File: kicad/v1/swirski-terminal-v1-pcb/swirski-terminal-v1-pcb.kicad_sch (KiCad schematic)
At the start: 15 parts, among them U1 Coin_Vibration_Motor, U1 Seeed_Lipo_Rider_Plus, U2 MAX17048

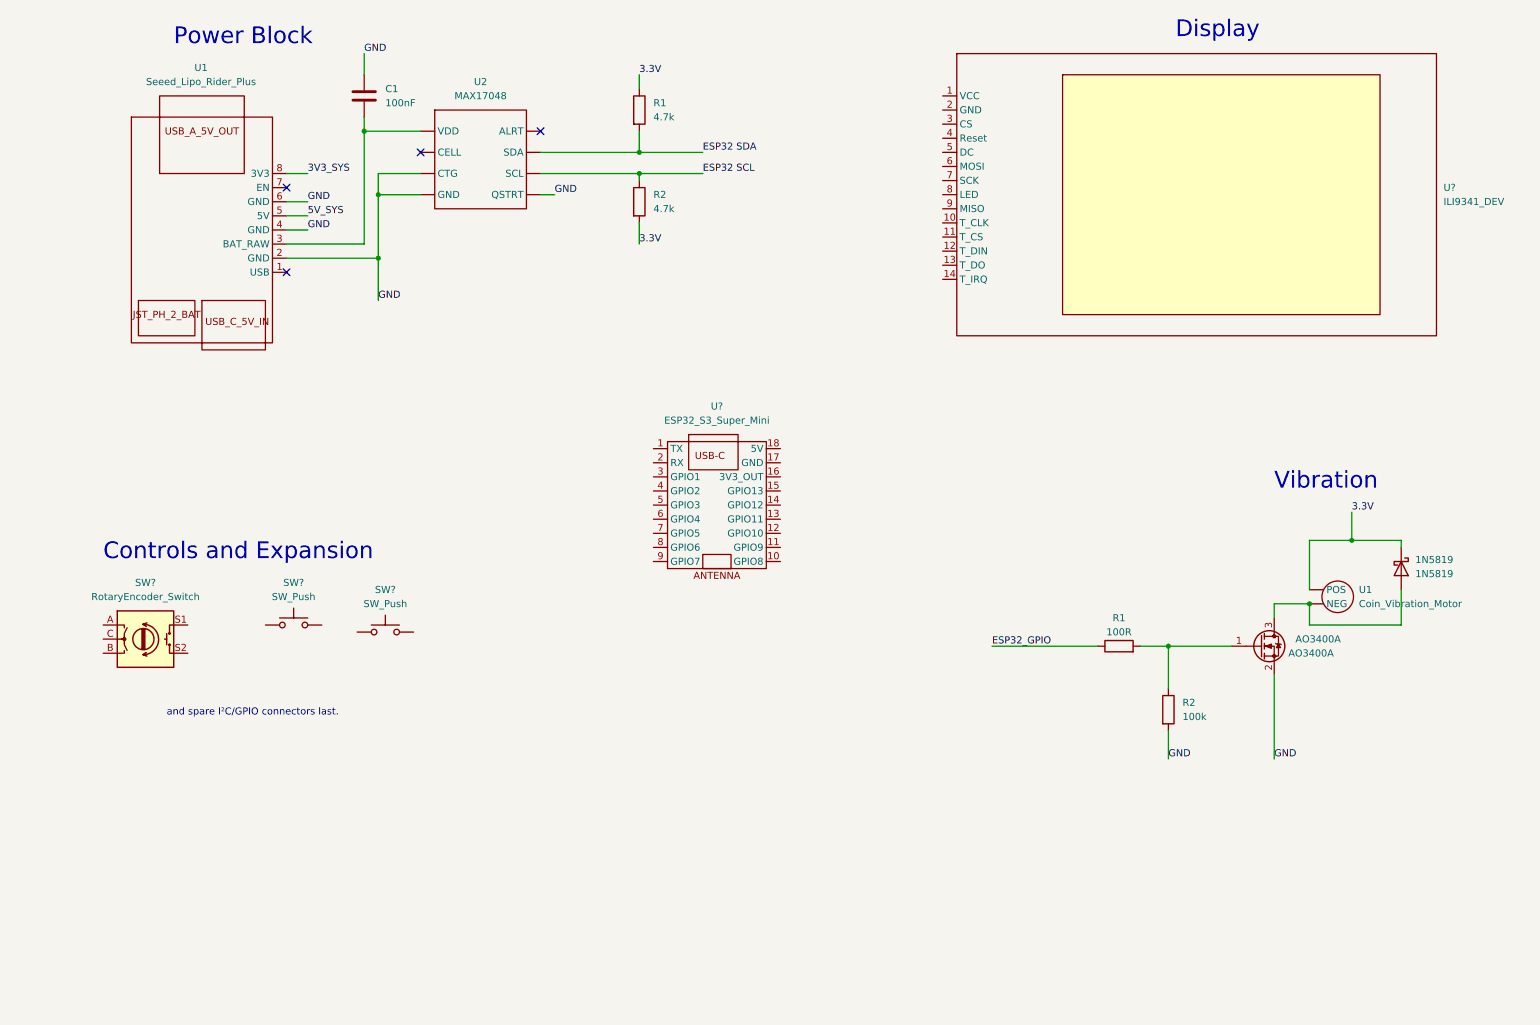
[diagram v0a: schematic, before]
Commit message: updated swirski terminal schematic!
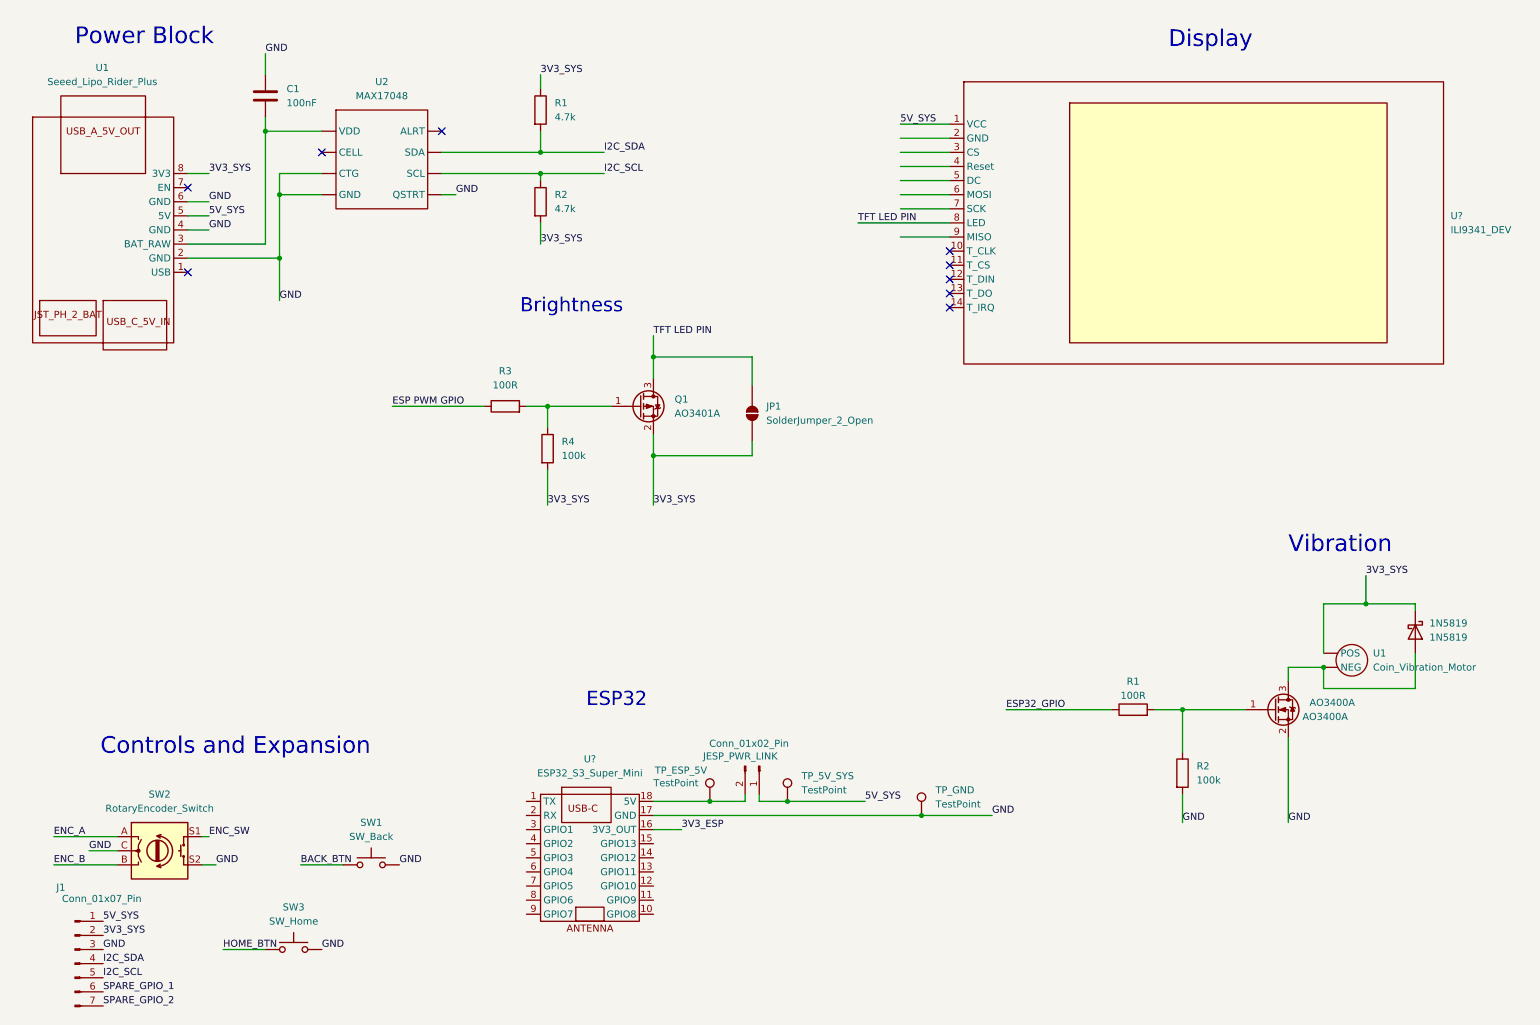
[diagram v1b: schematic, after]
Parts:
- added J1: Conn_01x07_Pin, symbol Connector:Conn_01x07_Pin
- added JESP_PWR_LINK: Conn_01x02_Pin, symbol Connector:Conn_01x02_Pin
- added JP1: SolderJumper_2_Open, symbol Jumper:SolderJumper_2_Open
- added Q1: AO3401A, Package_TO_SOT_SMD:SOT-23, symbol Transistor_FET:AO3401A
- added R3: 100R, symbol Device:R
- added R4: 100k, symbol Device:R
- added TP_5V_SYS, TP_ESP_5V, TP_GND: TestPoint, symbol Connector:TestPoint
- SW1: renamed from SW?; value SW_Push -> SW_Back
- SW3: renamed from SW?; value SW_Push -> SW_Home
- gave numbers to parts that had none: 1
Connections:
- net 3.3V is gone; now on net 3V3_SYS: 1N5819.1 (K), R1.1, R2.2, U1. (NEG)
- net ESP32 SDA is gone; now on net I2C_SDA: R1.2, U2. (QSTRT)
- net 3V3_SYS: now also J1.2 (Pin_2), JP1.1 (A), Q1.2 (S), R4.2
- net 5V_SYS: now also U?.1 (VCC), J1.1 (Pin_1), JESP_PWR_LINK.1 (Pin_1), TP_5V_SYS.1
- net GND: now also SW1.2, SW2.C, SW2.S2, SW3.2, U?.17 (GND), J1.3 (Pin_3), TP_GND.1
- net ENC_A: now reaches SW2.A
- net ENC_B: now reaches SW2.B
- net ENC_SW: now reaches SW2.S1
- net HOME_BTN: now reaches SW3.1
- net 3V3_ESP: now reaches U?.16 (3V3_OUT)
- net at U?.18 (5V): now also JESP_PWR_LINK.2 (Pin_2), TP_ESP_5V.1
- net TFT LED PIN: now reaches U?.8 (LED)
- net TFT LED PIN: now also JP1.2 (B), Q1.3 (D)
- net I2C_SDA: now reaches U2. (QSTRT)
- net I2C_SDA: now also J1.4 (Pin_4)
- net BACK_BTN: now reaches SW1.1
- net ESP32 SCL  renamed I2C_SCL
- net I2C_SCL: now also J1.5 (Pin_5)
- new net: Q1.1 (G), R3.2, R4.1
- new net ESP PWM GPIO: R3.1
- new net SPARE_GPIO_1: J1.6 (Pin_6)
- new net SPARE_GPIO_2: J1.7 (Pin_7)
- no-connect marks 4 -> 9
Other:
- note added: "Brightness"
- note added: "ESP32"
- note removed: "and spare I²C/GPIO connectors last."
- moved on the sheet: 1N5819, AO3400A, C1, R1, R2, SW1, SW2, SW3, U1, U2, U?

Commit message: PCB Updates
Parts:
- added C2, C4, C6, C8: 100nF, symbol Device:C
- added C3, C5, C7: 10µF, symbol Device:C
- added R5: 10k, symbol pspice:R
- added TP_3V3_ESP, TP_3V3_SYS, TP_BAT_RAW: TestPoint, symbol Connector:TestPoint
- added U3: MCP23008-xSO, Package_SO:SOIC-18W_7.5x11.6mm_P1.27mm, symbol Interface_Expansion:MCP23008-xSO
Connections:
- net ESP PWM GPIO is gone; now on net TFT_BL_PWM: R3.1
- net ESP32_GPIO is gone; now on net VIB_EN: R1.1
- net SPARE_GPIO_1 is gone; now on net ESP_SPARE_A: J1.6 (Pin_6)
- net 3V3_ESP: now also J1.2 (Pin_2), R1.1, R2.2, C2.1, R5.1, TP_3V3_ESP.1, U3.18 (VDD)
- net 3V3_SYS: now also C5.1, C6.1, C7.1, C8.1, TP_3V3_SYS.1; no longer J1.2 (Pin_2), R1.1, R2.2
- net 5V_SYS: now also C3.2, C4.2
- net BACK_BTN: now also U3.11 (GP1)
- net ENC_A: now also U?.13 (GPIO11)
- net ENC_B: now also U?.12 (GPIO10)
- net ENC_SW: now also U3.10 (GP0)
- net GND: now also U?.2 (GND), C2.2, C3.1, C4.1, C5.2, C6.2, C7.2, C8.2, U3.3 (A2), U3.4 (A1), U3.5 (A0), U3.9 (VSS)
- net HOME_BTN: now also U3.12 (GP2)
- net I2C_SCL: now also U?.3 (GPIO1), U3.1 (SCL)
- net I2C_SDA: now also U?.4 (GPIO2), U3.2 (SDA)
- net LCD_PIN_RST: now reaches U?.10 (GPIO8)
- net LCD_PIN_RST: now also U?.4 (Reset)
- net ESP_SPARE_A: now reaches U?.11 (GPIO9)
- net TFT_BL_PWM: now reaches U?.14 (GPIO12)
- net VIB_EN: now reaches U?.15 (GPIO13)
- net LCD_PIN_DC: now reaches U?.6 (GPIO4)
- net LCD_PIN_DC: now also U?.5 (DC)
- net LCD_PIN_CS: now reaches U?.7 (GPIO5)
- net LCD_PIN_CS: now also U?.3 (CS)
- net LCD_PIN_MOSI: now reaches U?.8 (GPIO6)
- net LCD_PIN_MOSI: now also U?.6 (MOSI)
- net LCD_PIN_SCLK: now reaches U?.9 (GPIO7)
- net LCD_PIN_SCLK: now also U?.7 (SCK)
- net at C1.2, U1.3 (BAT_RAW), U2. (QSTRT): now also TP_BAT_RAW.1
- net SPARE_GPIO_2 renamed EXTRA_GPIO_1
- net EXTRA_GPIO_1: now also U3.13 (GP3)
- new net: R5.2, U3.6 (~{RESET})
- new net EXTRA_GPIO_2: U3.14 (GP4)
- new net EXTRA_GPIO_3: U3.15 (GP5)
- new net EXTRA_GPIO_4: U3.16 (GP6)
- new net EXTRA_OUTPUT: U3.17 (GP7)
- no-connect marks 9 -> 14
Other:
- note added: "GPIO EXPANSION INTERNAL"
- moved on the sheet: JP1, Q1, R1, R2, R3, R4, TP_GND

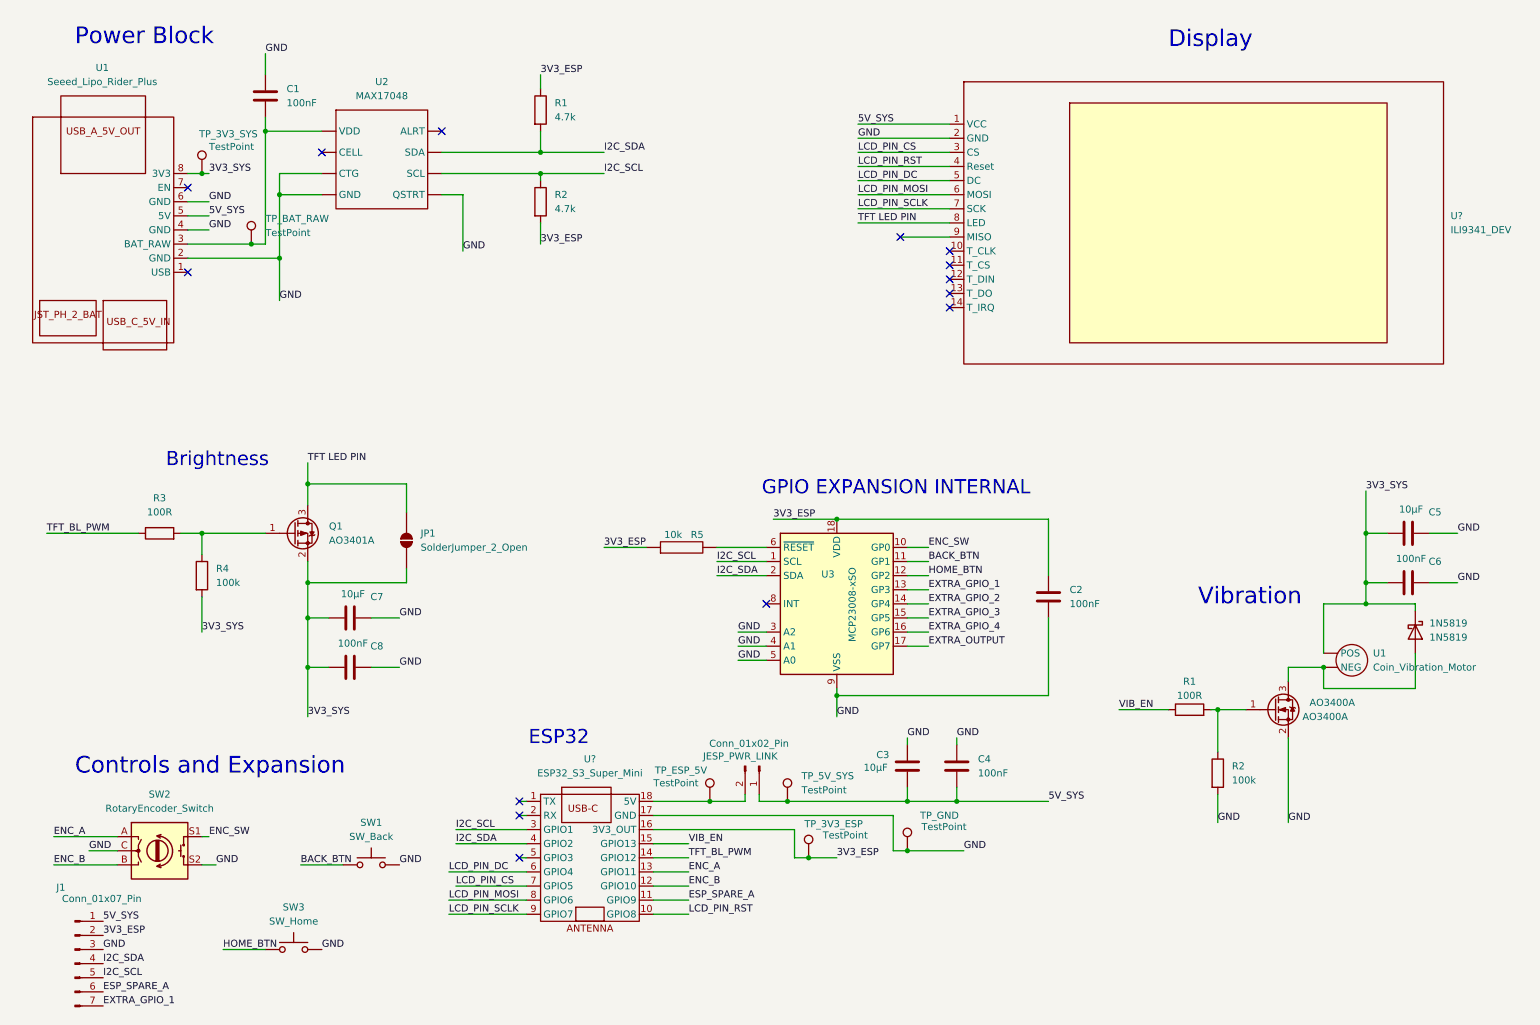
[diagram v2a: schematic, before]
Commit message: More Kicad updates - playing around with the schematic and replacing SMD components that were being used on the PCB
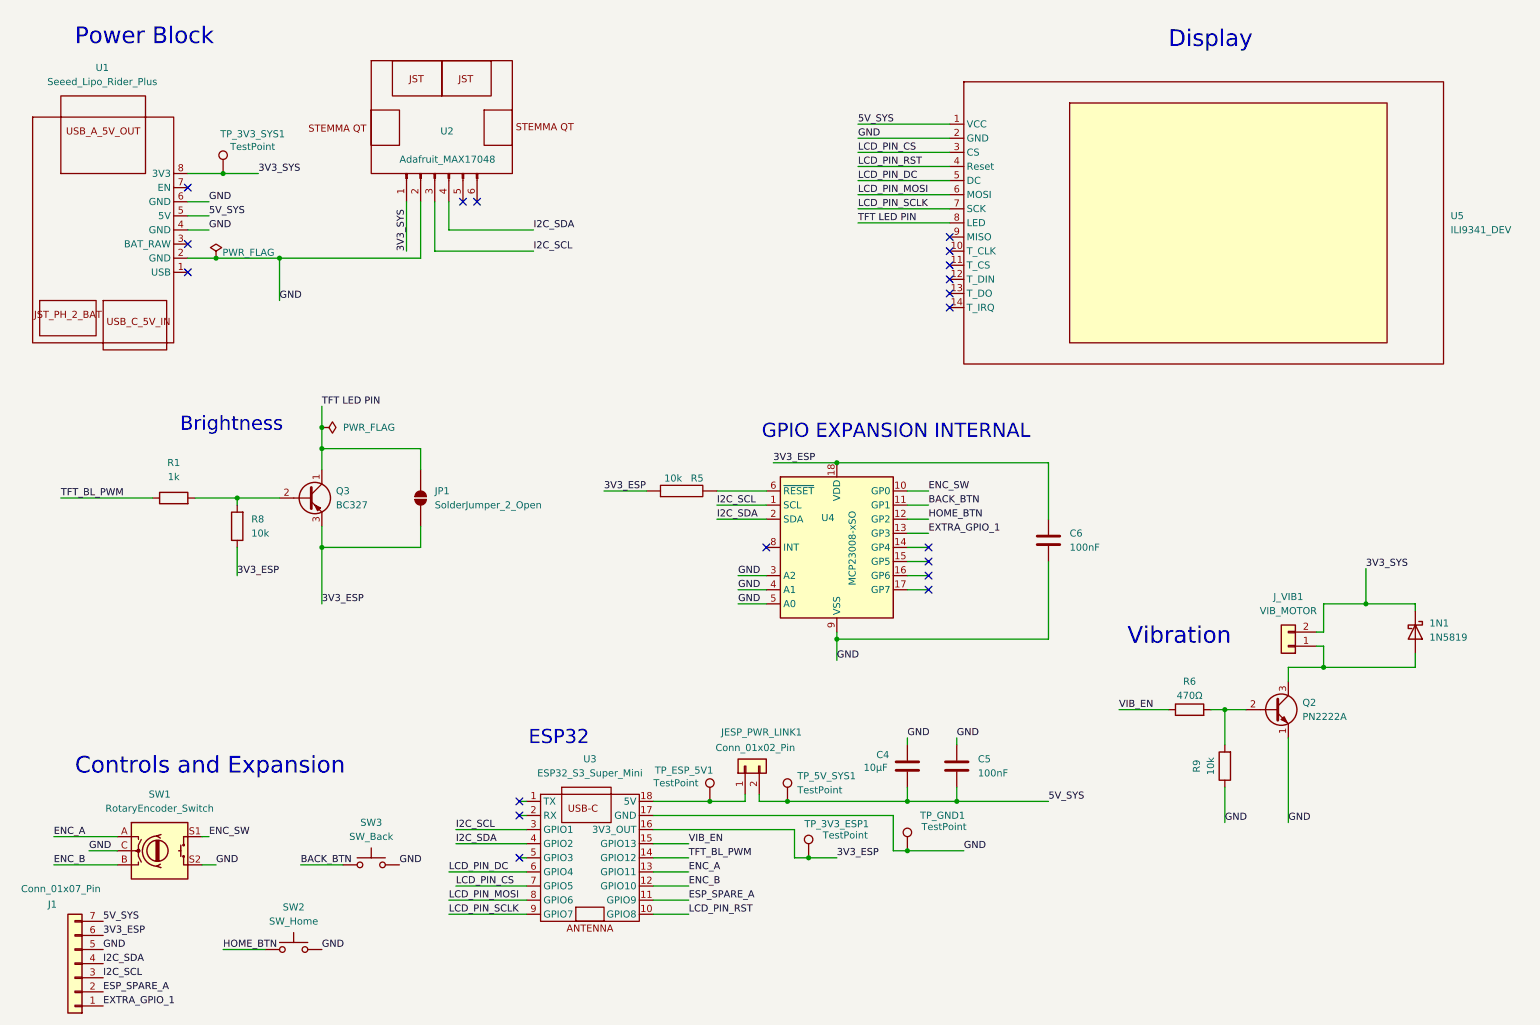
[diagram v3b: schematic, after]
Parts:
- removed AO3400A: AO3400A, Package_TO_SOT_SMD:SOT-23, symbol Transistor_FET:AO3400A
- removed C1, C6, C8: 100nF, symbol Device:C
- removed C5, C7: 10µF, symbol Device:C
- removed Q1: AO3401A, Package_TO_SOT_SMD:SOT-23, symbol Transistor_FET:AO3401A
- removed R1, R2: 4.7k, symbol Device:R
- removed R2, R4: 100k, symbol Device:R
- removed TP_BAT_RAW: TestPoint, symbol Connector:TestPoint
- removed U1: Coin_Vibration_Motor, symbol Swirski_Terminal:Coin_Vibration_Motor
- removed U2: MAX17048, symbol Swirski_Terminal:MAX17048
- added J_VIB1: VIB_MOTOR, Connector_PinHeader_2.54mm:PinHeader_1x02_P2.54mm_Vertical, symbol Connector_Generic:Conn_01x02
- added Q2: PN2222A, Package_TO_SOT_THT:TO-92_Inline, symbol Transistor_BJT:PN2222A
- added Q3: BC327, Package_TO_SOT_THT:TO-92_Inline, symbol Transistor_BJT:BC327
- added R8, R9: 10k, Resistor_THT:R_Axial_DIN0207_L6.3mm_D2.5mm_P10.16mm_Horizontal, symbol Device:R
- added U2: Adafruit_MAX17048, Swirski_Terminal:Adafruit_MAX17048_Breakout, symbol Swirski_Terminal:Adafruit_MAX17048
- C4: renamed from C3; footprint (none) -> Capacitor_THT:CP_Radial_D5.0mm_P2.00mm
- C5: renamed from C4; footprint (none) -> Capacitor_THT:C_Disc_D5.0mm_W2.5mm_P5.00mm
- C6: renamed from C2; footprint (none) -> Capacitor_THT:C_Disc_D5.0mm_W2.5mm_P5.00mm
- J1: footprint (none) -> Connector_PinHeader_2.54mm:PinHeader_1x07_P2.54mm_Vertical; symbol Connector:Conn_01x07_Pin -> Connector_Generic:Conn_01x07
- JESP_PWR_LINK1: renamed from JESP_PWR_LINK; footprint (none) -> Connector_PinHeader_2.54mm:PinHeader_1x02_P2.54mm_Vertical; symbol Connector:Conn_01x02_Pin -> Connector_Generic:Conn_01x02
- JP1: footprint (none) -> Connector_PinHeader_2.54mm:PinHeader_1x02_P2.54mm_Vertical
- R1: renamed from R3; value 100R -> 1k; footprint (none) -> Resistor_THT:R_Axial_DIN0207_L6.3mm_D2.5mm_P10.16mm_Horizontal
- R5: footprint (none) -> Resistor_THT:R_Axial_DIN0207_L6.3mm_D2.5mm_P10.16mm_Horizontal
- R6: renamed from R1; value 100R -> 470Ω; footprint (none) -> Resistor_THT:R_Axial_DIN0207_L6.3mm_D2.5mm_P10.16mm_Horizontal
- SW1: renamed from SW2; footprint (none) -> Rotary_Encoder:RotaryEncoder_Alps_EC11E-Switch_Vertical_H20mm
- SW2: renamed from SW3; footprint (none) -> Button_Switch_THT:SW_PUSH_6mm
- SW3: renamed from SW1; footprint (none) -> Button_Switch_THT:SW_PUSH_6mm
- TP_3V3_ESP1: renamed from TP_3V3_ESP; footprint (none) -> TestPoint:TestPoint_Loop_D2.50mm_Drill1.0mm
- TP_3V3_SYS1: renamed from TP_3V3_SYS; footprint (none) -> TestPoint:TestPoint_Loop_D2.50mm_Drill1.0mm
- TP_5V_SYS1: renamed from TP_5V_SYS; footprint (none) -> TestPoint:TestPoint_Loop_D2.50mm_Drill1.0mm
- TP_ESP_5V1: renamed from TP_ESP_5V; footprint (none) -> TestPoint:TestPoint_Loop_D2.50mm_Drill1.0mm
- TP_GND1: renamed from TP_GND; footprint (none) -> TestPoint:TestPoint_Loop_D2.50mm_Drill1.0mm
- U4: renamed from U3; footprint Package_SO:SOIC-18W_7.5x11.6mm_P1.27mm -> Package_DIP:DIP-18_W7.62mm
- gave numbers to parts that had none: 2
- renumbered 1N5819 to 1N1
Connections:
- net 3V3_ESP: now also J1.6 (Pin_6), JP1.1 (A), Q3.3 (E), R8.1; no longer J1.2 (Pin_2)
- net 3V3_SYS: now also J_VIB1.2 (Pin_2), U2.1 (VIN); no longer JP1.1 (A)
- net 5V_SYS: now also J1.7 (Pin_7), JESP_PWR_LINK1.2 (Pin_2); no longer J1.1 (Pin_1), JESP_PWR_LINK1.1 (Pin_1)
- net ESP_SPARE_A: now also J1.2 (Pin_2); no longer J1.6 (Pin_6)
- net EXTRA_GPIO_1: now also J1.1 (Pin_1); no longer J1.7 (Pin_7)
- net GND: now also J1.5 (Pin_5), Q2.1 (E), R9.1, U2.2 (GND); no longer J1.3 (Pin_3)
- net I2C_SCL: now also J1.3 (Pin_3), U2.3 (SCL); no longer J1.5 (Pin_5)
- net I2C_SDA: now also U2.4 (SDA)
- net TFT LED PIN: now also Q3.1 (C)
- net at R1.2: now also Q3.2 (B), R8.2
- net at TP_ESP_5V1.1, U3.18 (5V): now also JESP_PWR_LINK1.1 (Pin_1); no longer JESP_PWR_LINK1.2 (Pin_2)
- net at 1N1.2 (A): now also J_VIB1.1 (Pin_1), Q2.3 (C)
- net at R6.2: now also Q2.2 (B), R9.2
- net EXTRA_GPIO_2: no longer names the net of U4.14 (GP4)
- net EXTRA_GPIO_3: no longer names the net of U4.15 (GP5)
- net EXTRA_GPIO_4: no longer names the net of U4.16 (GP6)
- net EXTRA_OUTPUT: no longer names the net of U4.17 (GP7)
- no-connect marks 14 -> 19
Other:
- moved on the sheet: C6, JP1, R1, R5, TP_3V3_SYS1, U4

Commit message: Add lock file for KiCad schematic to prevent concurrent edits
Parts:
- removed J1: Conn_01x07_Pin, Connector_PinHeader_2.54mm:PinHeader_1x07_P2.54mm_Vertical, symbol Connector_Generic:Conn_01x07
- removed JESP_PWR_LINK1: Conn_01x02_Pin, Connector_PinHeader_2.54mm:PinHeader_1x02_P2.54mm_Vertical, symbol Connector_Generic:Conn_01x02
- added D1: 1N5819, Diode_THT:D_DO-41_SOD81_P10.16mm_Horizontal, symbol Diode:1N5819
- U4: value MCP23008-xSO -> MCP23008-E/P
- renumbered 1N1 to D2
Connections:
- net ESP_SPARE_A is gone; now on net I2C_SDA: U3.11 (GPIO9)
- net 3V3_ESP: now also U2.1 (VIN)
- net 3V3_SYS: no longer U2.1 (VIN)
- net 5V_SYS: now also D1.2 (A)
- net ENC_A: now also U4.15 (GP5); no longer U3.13 (GPIO11)
- net ENC_B: now also U4.14 (GP4); no longer U3.12 (GPIO10)
- net I2C_SCL: now also U3.10 (GPIO8); no longer U3.3 (GPIO1)
- net I2C_SDA: no longer U3.4 (GPIO2)
- net LCD_PIN_CS: now also U3.9 (GPIO7); no longer U3.7 (GPIO5)
- net LCD_PIN_DC: now also U3.7 (GPIO5); no longer U3.6 (GPIO4)
- net LCD_PIN_MOSI: now also U3.6 (GPIO4); no longer U3.8 (GPIO6)
- net LCD_PIN_RST: now also U3.8 (GPIO6); no longer U3.10 (GPIO8)
- net LCD_PIN_SCLK: now also U3.5 (GPIO3); no longer U3.9 (GPIO7)
- net TFT_BL_PWM: now also U3.3 (GPIO1); no longer U3.14 (GPIO12)
- net at TP_ESP_5V1.1, U3.18 (5V_IN): now also D1.1 (K)
- net EXTRA_GPIO_1: no longer names the net of U4.13 (GP3)
- no-connect marks 19 -> 21
